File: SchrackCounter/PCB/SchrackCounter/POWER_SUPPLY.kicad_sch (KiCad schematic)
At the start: 14 parts

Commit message: Schematic update
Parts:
- gave numbers to parts that had none: 14
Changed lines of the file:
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@@
 		(on_board yes)
 		(dnp no)
-		(property "Reference" "C?"
+		(property "Reference" "C4"
 			(at 171.45 66.04 0)
 			(effects
@@
 			(project "SchrackCounter"
 				(path "/d96f2ffc-3f4c-4f71-b693-29f6b8c3245d/2b0bd697-1473-4a31-8990-1278f12dea07"
-					(reference "C?")
+					(reference "C4")
 					(unit 1)
 				)
@@
 		(on_board yes)
 		(dnp no)
-		(property "Reference" "C?"
+		(property "Reference" "C7"
 			(at 208.28 66.04 0)
 			(effects
@@
 			(project "SchrackCounter"
 				(path "/d96f2ffc-3f4c-4f71-b693-29f6b8c3245d/2b0bd697-1473-4a31-8990-1278f12dea07"
-					(reference "C?")
+					(reference "C7")
 					(unit 1)
 				)
@@
 		(on_board yes)
 		(dnp no)
-		(property "Reference" "C?"
+		(property "Reference" "C2"
 			(at 125.095 123.19 0)
 			(effects
@@
 			(project "SchrackCounter"
 				(path "/d96f2ffc-3f4c-4f71-b693-29f6b8c3245d/2b0bd697-1473-4a31-8990-1278f12dea07"
-					(reference "C?")
+					(reference "C2")
 					(unit 1)
 				)
@@
 		(on_board yes)
 		(dnp no)
-		(property "Reference" "SW?"
+		(property "Reference" "SW1"
 			(at 200.66 121.92 0)
 			(effects
@@
 			(project "SchrackCounter"
 				(path "/d96f2ffc-3f4c-4f71-b693-29f6b8c3245d/2b0bd697-1473-4a31-8990-1278f12dea07"
-					(reference "SW?")
+					(reference "SW1")
 					(unit 1)
 				)
@@
 		(on_board yes)
 		(dnp no)
-		(property "Reference" "C?"
+		(property "Reference" "C8"
 			(at 217.805 66.04 0)
 			(effects
@@
 			(project "SchrackCounter"
 				(path "/d96f2ffc-3f4c-4f71-b693-29f6b8c3245d/2b0bd697-1473-4a31-8990-1278f12dea07"
-					(reference "C?")
+					(reference "C8")
 					(unit 1)
 				)
@@
 		(on_board yes)
 		(dnp no)
-		(property "Reference" "C?"
+		(property "Reference" "C1"
 			(at 114.935 123.19 0)
 			(effects
@@
 			(project "SchrackCounter"
 				(path "/d96f2ffc-3f4c-4f71-b693-29f6b8c3245d/2b0bd697-1473-4a31-8990-1278f12dea07"
-					(reference "C?")
+					(reference "C1")
 					(unit 1)
 				)
@@
 		(on_board yes)
 		(dnp no)
-		(property "Reference" "L?"
+		(property "Reference" "L1"
 			(at 168.275 54.61 90)
 			(effects
@@
 			(project "SchrackCounter"
 				(path "/d96f2ffc-3f4c-4f71-b693-29f6b8c3245d/2b0bd697-1473-4a31-8990-1278f12dea07"
-					(reference "L?")
+					(reference "L1")
 					(unit 1)
 				)
@@
 		(on_board yes)
 		(dnp no)
-		(property "Reference" "C?"
+		(property "Reference" "C6"
 			(at 198.12 66.04 0)
 			(effects
@@
 			(project "SchrackCounter"
 				(path "/d96f2ffc-3f4c-4f71-b693-29f6b8c3245d/2b0bd697-1473-4a31-8990-1278f12dea07"
-					(reference "C?")
+					(reference "C6")
 					(unit 1)
 				)
@@
 		(on_board yes)
 		(dnp no)
-		(property "Reference" "R?"
+		(property "Reference" "R1"
 			(at 137.16 69.85 90)
 			(effects
@@
 			(project "SchrackCounter"
 				(path "/d96f2ffc-3f4c-4f71-b693-29f6b8c3245d/2b0bd697-1473-4a31-8990-1278f12dea07"
-					(reference "R?")
+					(reference "R1")
 					(unit 1)
 				)
@@
 		(on_board yes)
 		(dnp no)
-		(property "Reference" "C?"
+		(property "Reference" "C3"
 			(at 161.29 66.04 0)
 			(effects
@@
 			(project "SchrackCounter"
 				(path "/d96f2ffc-3f4c-4f71-b693-29f6b8c3245d/2b0bd697-1473-4a31-8990-1278f12dea07"
-					(reference "C?")
+					(reference "C3")
 					(unit 1)
 				)
@@
 		(on_board yes)
 		(dnp no)
-		(property "Reference" "BT?"
+		(property "Reference" "BT1"
 			(at 136.525 123.19 0)
 			(effects
@@
 			(project "SchrackCounter"
 				(path "/d96f2ffc-3f4c-4f71-b693-29f6b8c3245d/2b0bd697-1473-4a31-8990-1278f12dea07"
-					(reference "BT?")
+					(reference "BT1")
 					(unit 1)
 				)
@@
 		(on_board yes)
 		(dnp no)
-		(property "Reference" "R?"
+		(property "Reference" "R2"
 			(at 146.685 69.85 90)
 			(effects
@@
 			(project "SchrackCounter"
 				(path "/d96f2ffc-3f4c-4f71-b693-29f6b8c3245d/2b0bd697-1473-4a31-8990-1278f12dea07"
-					(reference "R?")
+					(reference "R2")
 					(unit 1)
 				)
@@
 		(on_board yes)
 		(dnp no)
-		(property "Reference" "IC?"
+		(property "Reference" "IC1"
 			(at 140.97 50.165 0)
 			(effects
@@
 			(project "SchrackCounter"
 				(path "/d96f2ffc-3f4c-4f71-b693-29f6b8c3245d/2b0bd697-1473-4a31-8990-1278f12dea07"
-					(reference "IC?")
+					(reference "IC1")
 					(unit 1)
 				)
@@
 		(on_board yes)
 		(dnp no)
-		(property "Reference" "C?"
+		(property "Reference" "C5"
 			(at 187.96 66.04 0)
 			(effects
@@
 			(project "SchrackCounter"
 				(path "/d96f2ffc-3f4c-4f71-b693-29f6b8c3245d/2b0bd697-1473-4a31-8990-1278f12dea07"
-					(reference "C?")
-					(unit 1)
-				)
+					(reference "C5")
+					(unit 1)
+				)

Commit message: Schematic update
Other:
- moved on the sheet: BT1, C1, C2, SW1A
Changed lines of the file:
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@@
 	)
 	(junction
-		(at 111.76 129.54)
+		(at 110.49 127)
 		(diameter 0)
 		(color 0 0 0 0)
@@
 	)
 	(junction
-		(at 121.92 119.38)
+		(at 120.65 116.84)
 		(diameter 0)
 		(color 0 0 0 0)
@@
 	)
 	(junction
-		(at 121.92 129.54)
+		(at 120.65 127)
 		(diameter 0)
 		(color 0 0 0 0)
@@
 	)
 	(junction
-		(at 111.76 119.38)
+		(at 110.49 116.84)
 		(diameter 0)
 		(color 0 0 0 0)
@@
 	)
 	(no_connect
-		(at 210.82 119.38)
-	)
-	(wire
-		(pts
-			(xy 100.33 123.19) (xy 107.95 123.19)
+		(at 209.55 120.65)
+	)
+	(wire
+		(pts
+			(xy 99.06 120.65) (xy 106.68 120.65)
 		)
 		(stroke
@@
 	(wire
 		(pts
-			(xy 210.82 119.38) (xy 205.74 119.38)
+			(xy 209.55 120.65) (xy 204.47 120.65)
 		)
 		(stroke
@@
 	(wire
 		(pts
-			(xy 111.76 129.54) (xy 121.92 129.54)
+			(xy 110.49 127) (xy 120.65 127)
 		)
 		(stroke
@@
 	(wire
 		(pts
-			(xy 190.5 116.84) (xy 195.58 116.84)
+			(xy 189.23 118.11) (xy 194.31 118.11)
 		)
 		(stroke
@@
 	(wire
 		(pts
-			(xy 121.92 119.38) (xy 121.92 120.65)
-		)
-		(stroke
-			(width 0)
-			(type default)
-		)
-	)
-	(wire
-		(pts
-			(xy 107.95 129.54) (xy 111.76 129.54)
+			(xy 120.65 116.84) (xy 120.65 118.11)
+		)
+		(stroke
+			(width 0)
+			(type default)
+		)
+	)
+	(wire
+		(pts
+			(xy 106.68 127) (xy 110.49 127)
 		)
 		(stroke
@@
 	(wire
 		(pts
-			(xy 100.33 125.73) (xy 107.95 125.73)
+			(xy 99.06 123.19) (xy 106.68 123.19)
 		)
 		(stroke
@@
 	(wire
 		(pts
-			(xy 107.95 125.73) (xy 107.95 129.54)
+			(xy 106.68 123.19) (xy 106.68 127)
 		)
 		(stroke
@@
 	(wire
 		(pts
-			(xy 107.95 123.19) (xy 107.95 119.38)
+			(xy 106.68 120.65) (xy 106.68 116.84)
 		)
 		(stroke
@@
 	(wire
 		(pts
-			(xy 111.76 119.38) (xy 111.76 120.65)
+			(xy 110.49 116.84) (xy 110.49 118.11)
 		)
 		(stroke
@@
 	(wire
 		(pts
-			(xy 107.95 119.38) (xy 111.76 119.38)
+			(xy 106.68 116.84) (xy 110.49 116.84)
 		)
 		(stroke
@@
 	(wire
 		(pts
-			(xy 121.92 119.38) (xy 133.35 119.38)
+			(xy 120.65 116.84) (xy 132.08 116.84)
 		)
 		(stroke
@@
 	(wire
 		(pts
-			(xy 111.76 119.38) (xy 121.92 119.38)
+			(xy 110.49 116.84) (xy 120.65 116.84)
 		)
 		(stroke
@@
 	(wire
 		(pts
-			(xy 121.92 128.27) (xy 121.92 129.54)
+			(xy 120.65 125.73) (xy 120.65 127)
 		)
 		(stroke
@@
 	(wire
 		(pts
-			(xy 121.92 129.54) (xy 133.35 129.54)
+			(xy 120.65 127) (xy 132.08 127)
 		)
 		(stroke
@@
 	(wire
 		(pts
-			(xy 111.76 128.27) (xy 111.76 129.54)
-		)
-		(stroke
-			(width 0)
-			(type default)
-		)
-	)
-	(wire
-		(pts
-			(xy 209.55 114.3) (xy 205.74 114.3)
+			(xy 110.49 125.73) (xy 110.49 127)
+		)
+		(stroke
+			(width 0)
+			(type default)
+		)
+	)
+	(wire
+		(pts
+			(xy 208.28 115.57) (xy 204.47 115.57)
 		)
 		(stroke
@@
 	(global_label "VBATT"
 		(shape input)
-		(at 190.5 116.84 180)
+		(at 189.23 118.11 180)
 		(fields_autoplaced yes)
 		(effects
@@
 		)
 		(property "Intersheetrefs" "${INTERSHEET_REFS}"
-			(at 184.284 116.84 0)
+			(at 183.014 118.11 0)
 			(effects
 				(font
@@
 	(global_label "VBATT"
 		(shape input)
-		(at 100.33 123.19 180)
+		(at 99.06 120.65 180)
 		(fields_autoplaced yes)
 		(effects
@@
 		)
 		(property "Intersheetrefs" "${INTERSHEET_REFS}"
-			(at 94.114 123.19 0)
+			(at 92.844 120.65 0)
 			(effects
 				(font
@@
 	(symbol
 		(lib_id "power:+5V")
-		(at 209.55 114.3 270)
+		(at 208.28 115.57 270)
 		(unit 1)
 		(exclude_from_sim no)
@@
 		(fields_autoplaced yes)
 		(property "Reference" "#PWR02"
-			(at 205.74 114.3 0)
+			(at 204.47 115.57 0)
 			(effects
 				(font
@@
 		)
 		(property "Value" "+5V"
-			(at 213.36 114.2999 90)
+			(at 212.09 115.5699 90)
 			(effects
 				(font
@@
 		)
 		(property "Footprint" ""
-			(at 209.55 114.3 0)
+			(at 208.28 115.57 0)
 			(effects
 				(font
@@
 		)
 		(property "Datasheet" ""
-			(at 209.55 114.3 0)
+			(at 208.28 115.57 0)
 			(effects
 				(font
@@
 		)
 		(property "Description" "Power symbol creates a global label with name \"+5V\""
-			(at 209.55 114.3 0)
+			(at 208.28 115.57 0)
 			(effects
 				(font
@@
 	(symbol
 		(lib_id "power:GND")
-		(at 100.33 125.73 0)
+		(at 99.06 123.19 0)
 		(unit 1)
 		(exclude_from_sim no)
@@
 		(fields_autoplaced yes)
 		(property "Reference" "#PWR01"
-			(at 100.33 132.08 0)
+			(at 99.06 129.54 0)
 			(effects
 				(font
@@
 		)
 		(property "Value" "GND"
-			(at 100.33 130.81 0)
+			(at 99.06 128.27 0)
 			(effects
 				(font
@@
 		)
 		(property "Footprint" ""
-			(at 100.33 125.73 0)
+			(at 99.06 123.19 0)
 			(effects
 				(font
@@
 		)
 		(property "Datasheet" ""
-			(at 100.33 125.73 0)
+			(at 99.06 123.19 0)
 			(effects
 				(font
@@
 		)
 		(property "Description" "Power symbol creates a global label with name \"GND\" , ground"
-			(at 100.33 125.73 0)
+			(at 99.06 123.19 0)
 			(effects
 				(font
@@
 	(symbol
 		(lib_id "Device:C")
-		(at 121.92 124.46 0)
+		(at 120.65 121.92 0)
 		(unit 1)
 		(exclude_from_sim no)
@@
 		(dnp no)
 		(property "Reference" "C2"
-			(at 125.095 123.19 0)
+			(at 123.825 120.65 0)
 			(effects
 				(font
@@
 		)
 		(property "Value" "100nF"
-			(at 125.095 125.73 0)
+			(at 123.825 123.19 0)
 			(effects
 				(font
@@
 		)
 		(property "Footprint" "Capacitor_SMD:C_0805_2012Metric_Pad1.18x1.45mm_HandSolder"
-			(at 122.8852 128.27 0)
+			(at 121.6152 125.73 0)
 			(effects
 				(font
@@
 		)
 		(property "Datasheet" "~"
-			(at 121.92 124.46 0)
+			(at 120.65 121.92 0)
 			(effects
 				(font
@@
 		)
 		(property "Description" "Unpolarized capacitor"
-			(at 121.92 124.46 0)
+			(at 120.65 121.92 0)
 			(effects
 				(font
@@
 	(symbol
 		(lib_id "Switch:SW_DPDT_x2")
-		(at 200.66 116.84 0)
+		(at 199.39 118.11 0)
 		(unit 1)
 		(exclude_from_sim no)
@@
 		(dnp no)
 		(property "Reference" "SW1"
-			(at 200.66 121.92 0)
+			(at 199.39 123.19 0)
 			(effects
 				(font
@@
 		)
 		(property "Value" "SW_DPDT_x2"
-			(at 200.66 111.76 0)
+			(at 199.39 113.03 0)
 			(effects
 				(font
@@
 		)
 		(property "Footprint" "sumec_brd:Custom_SPDT_4.7mm_Switch"
-			(at 200.66 116.84 0)
+			(at 199.39 118.11 0)
 			(effects
 				(font
@@
 		)
 		(property "Datasheet" "https://cz.mouser.com/ProductDetail/E-Switch/500SSP1S1M2QEA?qs=rR7wk9eDIwofjM3j2mZRnA%3D%3D"
-			(at 200.66 116.84 0)
+			(at 199.39 118.11 0)
 			(effects
 				(font
@@
 		)
 		(property "Description" ""
-			(at 200.66 116.84 0)
+			(at 199.39 118.11 0)
 			(effects
 				(font
@@
 	(symbol
 		(lib_id "Device:C_Polarized")
-		(at 111.76 124.46 0)
+		(at 110.49 121.92 0)
 		(unit 1)
 		(exclude_from_sim no)
@@
 		(dnp no)
 		(property "Reference" "C1"
-			(at 114.935 123.19 0)
+			(at 113.665 120.65 0)
 			(effects
 				(font
@@
 		)
 		(property "Value" "10uF"
-			(at 114.935 125.73 0)
+			(at 113.665 123.19 0)
 			(effects
 				(font
@@
 		)
 		(property "Footprint" "Capacitor_Tantalum_SMD:CP_EIA-3216-18_Kemet-A_Pad1.58x1.35mm_HandSolder"
-			(at 112.7252 128.27 0)
+			(at 111.4552 125.73 0)
 			(effects
 				(font
@@
 		)
 		(property "Datasheet" "~"
-			(at 111.76 124.46 0)
+			(at 110.49 121.92 0)
 			(effects
 				(font
@@
 		)
 		(property "Description" "Polarized capacitor"
-			(at 111.76 124.46 0)
+			(at 110.49 121.92 0)
 			(effects
 				(font
@@
 	(symbol
 		(lib_id "Device:Battery")
-		(at 133.35 124.46 0)
+		(at 132.08 121.92 0)
 		(unit 1)
 		(exclude_from_sim no)
@@
 		(dnp no)
 		(property "Reference" "BT1"
-			(at 136.525 123.19 0)
+			(at 135.255 120.65 0)
 			(effects
 				(font
@@
 		)
 		(property "Value" "Battery"
-			(at 136.525 125.73 0)
+			(at 135.255 123.19 0)
 			(effects
 				(font
@@
 		)
 		(property "Footprint" "Battery:BatteryHolder_Keystone_2462_2xAA - no holes"
-			(at 133.35 122.936 90)
+			(at 132.08 120.396 90)
 			(effects
 				(font
@@
 		)
 		(property "Datasheet" "~"
-			(at 133.35 122.936 90)
+			(at 132.08 120.396 90)
 			(effects
 				(font
@@
 		)
 		(property "Description" "Multiple-cell battery"
-			(at 133.35 124.46 0)
-			(effects
-				(font
+			(at 132.08 121.92 0)
+			(effects
+				(font

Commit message: sleep, overated imo
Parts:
- BT1: footprint Battery:BatteryHolder_Keystone_2462_2xAA - no holes -> Connector_Samtec_HPM_THT:Samtec_HPM-02-01-x-S_Straight_1x02_Pitch5.08mm
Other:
- note added: "Batt connector should probs be in the box but not on the pcb"
- moved on the sheet: BT1, C1, C2, SW1A

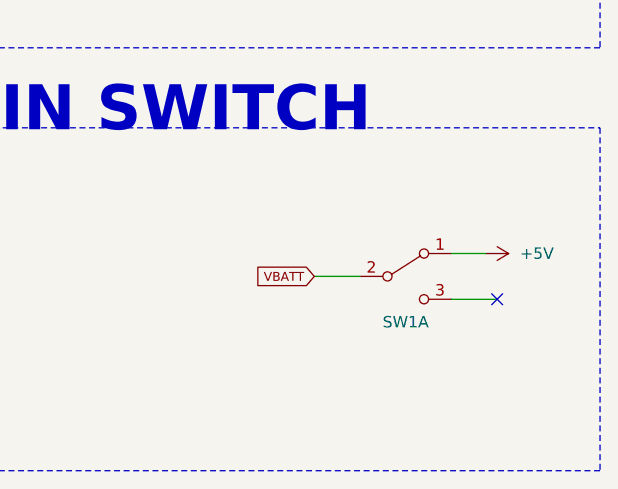
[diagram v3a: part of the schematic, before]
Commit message: SD card addition
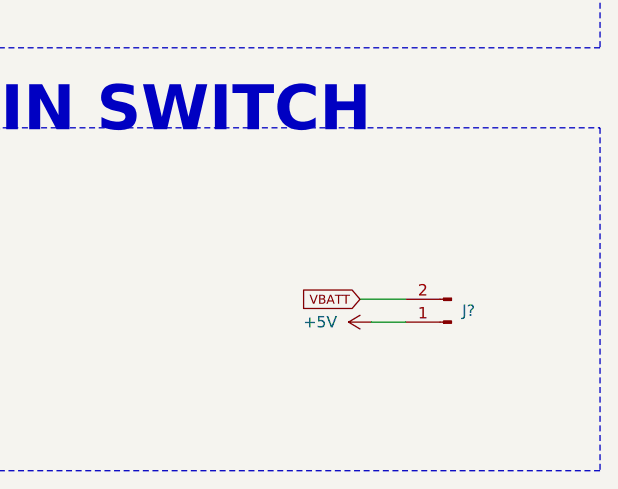
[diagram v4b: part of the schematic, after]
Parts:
- removed SW1: SW_DPDT_x2, sumec_brd:Custom_SPDT_4.7mm_Switch, symbol Switch:SW_DPDT_x2
- added J?: Conn_01x02_Pin, Connector_JST:JST_XH_B2B-XH-A_1x02_P2.50mm_Vertical, symbol Connector:Conn_01x02_Pin
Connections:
- net +5V: now also J?.1 (Pin_1)
- net VBATT: now also J?.2 (Pin_2)
- no-connect marks 1 -> 0
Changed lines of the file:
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@@
 		(color 0 0 0 0)
-	)
-	(no_connect
-		(at 223.52 114.3)
 	)
 	(wire
@@
 	(wire
 		(pts
-			(xy 223.52 114.3) (xy 218.44 114.3)
-		)
-		(stroke
-			(width 0)
-			(type default)
-		)
-	)
-	(wire
-		(pts
 			(xy 185.42 71.12) (xy 185.42 73.66)
 		)
@@
 	(wire
 		(pts
-			(xy 203.2 111.76) (xy 208.28 111.76)
+			(xy 208.28 114.3) (xy 213.36 114.3)
 		)
 		(stroke
@@
 	(wire
 		(pts
-			(xy 222.25 109.22) (xy 218.44 109.22)
+			(xy 209.55 116.84) (xy 213.36 116.84)
 		)
 		(stroke
@@
 	(global_label "VBATT"
 		(shape input)
-		(at 203.2 111.76 180)
+		(at 208.28 114.3 180)
 		(fields_autoplaced yes)
 		(effects
@@
 		)
 		(property "Intersheetrefs" "${INTERSHEET_REFS}"
-			(at 196.984 111.76 0)
+			(at 202.064 114.3 0)
 			(effects
 				(font
@@
 	(symbol
 		(lib_id "power:+5V")
-		(at 222.25 109.22 270)
+		(at 209.55 116.84 90)
 		(unit 1)
 		(exclude_from_sim no)
@@
 		(fields_autoplaced yes)
 		(property "Reference" "#PWR011"
-			(at 218.44 109.22 0)
+			(at 213.36 116.84 0)
 			(effects
 				(font
@@
 		)
 		(property "Value" "+5V"
-			(at 226.06 109.2199 90)
+			(at 205.74 116.8401 90)
 			(effects
 				(font
@@
 		)
 		(property "Footprint" ""
-			(at 222.25 109.22 0)
+			(at 209.55 116.84 0)
 			(effects
 				(font
@@
 		)
 		(property "Datasheet" ""
-			(at 222.25 109.22 0)
+			(at 209.55 116.84 0)
 			(effects
 				(font
@@
 		)
 		(property "Description" "Power symbol creates a global label with name \"+5V\""
-			(at 222.25 109.22 0)
+			(at 209.55 116.84 0)
 			(effects
 				(font
@@
 	)
 	(symbol
-		(lib_id "Switch:SW_DPDT_x2")
-		(at 213.36 111.76 0)
-		(unit 1)
-		(exclude_from_sim no)
-		(in_bom yes)
-		(on_board yes)
-		(dnp no)
-		(property "Reference" "SW1"
-			(at 213.36 116.84 0)
-			(effects
-				(font
-					(face "Bahnschrift")
-					(size 1.27 1.27)
-				)
-			)
-		)
-		(property "Value" "SW_DPDT_x2"
-			(at 213.36 106.68 0)
-			(effects
-				(font
-					(face "Bahnschrift")
-					(size 1.27 1.27)
-				)
-				(hide yes)
-			)
-		)
-		(property "Footprint" "sumec_brd:Custom_SPDT_4.7mm_Switch"
-			(at 213.36 111.76 0)
-			(effects
-				(font
-					(face "Bahnschrift")
-					(size 1.27 1.27)
-				)
-				(hide yes)
-			)
-		)
-		(property "Datasheet" "https://cz.mouser.com/ProductDetail/E-Switch/500SSP1S1M2QEA?qs=rR7wk9eDIwofjM3j2mZRnA%3D%3D"
-			(at 213.36 111.76 0)
-			(effects
-				(font
-					(face "Bahnschrift")
-					(size 1.27 1.27)
-				)
-				(hide yes)
-			)
-		)
-		(property "Description" ""
-			(at 213.36 111.76 0)
-			(effects
-				(font
-					(size 1.27 1.27)
-				)
-				(hide yes)
-			)
-		)
-		(pin "1"
-		)
-		(pin "2"
-		)
-		(pin "3"
-		)
-		(pin "4"
-		)
-		(pin "5"
-		)
-		(pin "6"
-		)
-		(instances
-			(project "SchrackCounter"
-				(path "/d96f2ffc-3f4c-4f71-b693-29f6b8c3245d/2b0bd697-1473-4a31-8990-1278f12dea07"
-					(reference "SW1")
-					(unit 1)
-				)
-			)
-		)
-	)
-	(symbol
 		(lib_id "Device:C")
 		(at 214.63 67.31 0)
@@
 					(unit 1)
 				)
+			)
+		)
+	)
+	(symbol
+		(lib_id "Connector:Conn_01x02_Pin")
+		(at 218.44 116.84 180)
+		(unit 1)
+		(exclude_from_sim no)
+		(in_bom yes)
+		(on_board yes)
+		(dnp no)
+		(property "Reference" "J?"
+			(at 220.345 115.57 0)
+			(effects
+				(font
+					(size 1.27 1.27)
+				)
+			)
+		)
+		(property "Value" "Conn_01x02_Pin"
+			(at 219.075 119.38 0)
+			(effects
+				(font
+					(size 1.27 1.27)
+				)
+				(hide yes)
+			)
+		)
+		(property "Footprint" "Connector_JST:JST_XH_B2B-XH-A_1x02_P2.50mm_Vertical"
+			(at 218.44 116.84 0)
+			(effects
+				(font
+					(size 1.27 1.27)
+				)
+				(hide yes)
+			)
+		)
+		(property "Datasheet" "~"
+			(at 218.44 116.84 0)
+			(effects
+				(font
+					(size 1.27 1.27)
+				)
+				(hide yes)
+			)
+		)
+		(property "Description" "Generic connector, single row, 01x02, script generated"
+			(at 218.44 116.84 0)
+			(effects
+				(font
+					(size 1.27 1.27)
+				)
+				(hide yes)
+			)
+		)
+		(pin "2"
+		)
+		(pin "1"
+		)
+		(instances
+			(project "SchrackCounter"
+				(path "/d96f2ffc-3f4c-4f71-b693-29f6b8c3245d/2b0bd697-1473-4a31-8990-1278f12dea07"
+					(reference "J?")
+					(unit 1)
+				)

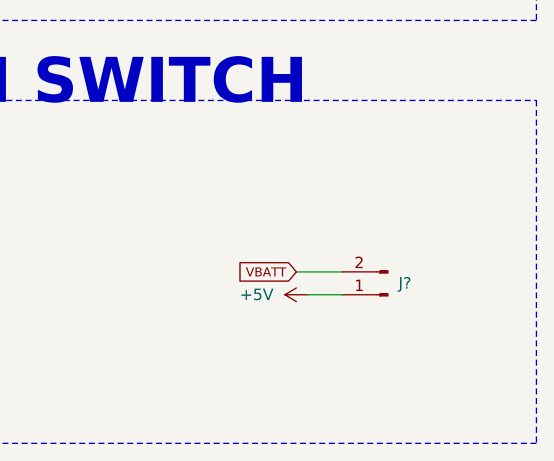
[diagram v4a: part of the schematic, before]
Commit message: Footprint reorder, schematic and pcb update
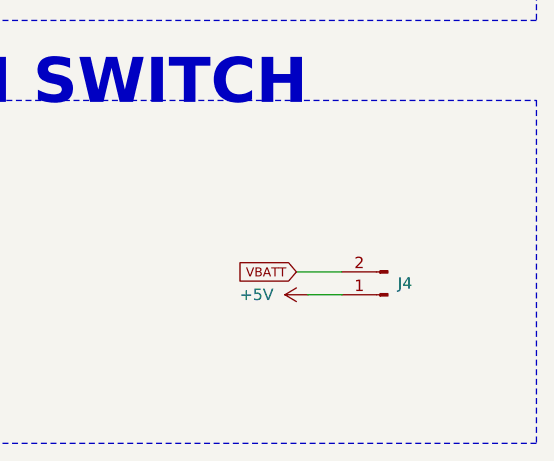
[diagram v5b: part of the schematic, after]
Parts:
- gave numbers to parts that had none: 1
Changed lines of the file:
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@@
 		(on_board yes)
 		(dnp no)
-		(property "Reference" "J?"
+		(property "Reference" "J4"
 			(at 220.345 115.57 0)
 			(effects
@@
 			(project "SchrackCounter"
 				(path "/d96f2ffc-3f4c-4f71-b693-29f6b8c3245d/2b0bd697-1473-4a31-8990-1278f12dea07"
-					(reference "J?")
+					(reference "J4")
 					(unit 1)
 				)

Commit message: PCB update
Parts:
- BT1: footprint Connector_Samtec_HPM_THT:Samtec_HPM-02-01-x-S_Straight_1x02_Pitch5.08mm -> Schrack_brd:SOLDER_PADS
- renumbered J4 to J1
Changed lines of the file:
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@@
 		(dnp no)
 		(fields_autoplaced yes)
-		(property "Reference" "#PWR011"
+		(property "Reference" "#PWR010"
 			(at 213.36 116.84 0)
 			(effects
@@
 			(project "SchrackCounter"
 				(path "/d96f2ffc-3f4c-4f71-b693-29f6b8c3245d/2b0bd697-1473-4a31-8990-1278f12dea07"
-					(reference "#PWR011")
+					(reference "#PWR010")
 					(unit 1)
 				)
@@
 		(on_board yes)
 		(dnp no)
-		(property "Reference" "#PWR010"
+		(property "Reference" "#PWR011"
 			(at 217.17 59.69 0)
 			(effects
@@
 			(project "SchrackCounter"
 				(path "/d96f2ffc-3f4c-4f71-b693-29f6b8c3245d/2b0bd697-1473-4a31-8990-1278f12dea07"
-					(reference "#PWR010")
+					(reference "#PWR011")
 					(unit 1)
 				)
@@
 			)
 		)
-		(property "Footprint" "Connector_Samtec_HPM_THT:Samtec_HPM-02-01-x-S_Straight_1x02_Pitch5.08mm"
+		(property "Footprint" "Schrack_brd:SOLDER_PADS"
 			(at 132.08 119.126 90)
 			(effects
@@
 		(on_board yes)
 		(dnp no)
-		(property "Reference" "J4"
+		(property "Reference" "J1"
 			(at 220.345 115.57 0)
 			(effects
@@
 			(project "SchrackCounter"
 				(path "/d96f2ffc-3f4c-4f71-b693-29f6b8c3245d/2b0bd697-1473-4a31-8990-1278f12dea07"
-					(reference "J4")
-					(unit 1)
-				)
+					(reference "J1")
+					(unit 1)
+				)

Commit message: schematic and board update
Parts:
- removed C3, C5, C6, C7: 22uF, Capacitor_Tantalum_SMD:CP_EIA-2012-12_Kemet-R_Pad1.30x1.05mm_HandSolder, symbol Device:C_Polarized
- removed C4: 100nF.vin, Capacitor_SMD:C_0805_2012Metric_Pad1.18x1.45mm_HandSolder, symbol Device:C
- removed C8: 100nF.vout, Capacitor_SMD:C_0805_2012Metric_Pad1.18x1.45mm_HandSolder, symbol Device:C
- removed IC1: TPS565242DRLR, Package_TO_SOT_SMD:SOT-563, symbol SamacSys_Parts:TPS565242DRLR
- removed L1: 1.5uH, Inductor_SMD:L_Vishay_IHLP-1212, symbol Device:L
- removed R1: 45k, Resistor_SMD:R_0805_2012Metric_Pad1.20x1.40mm_HandSolder, symbol Device:R
- removed R2: 10k, Resistor_SMD:R_0805_2012Metric_Pad1.20x1.40mm_HandSolder, symbol Device:R
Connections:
- net +5V: now also J1.2 (Pin_2); no longer J1.1 (Pin_1)
- net VBATT: now also J1.1 (Pin_1); no longer J1.2 (Pin_2)
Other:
- note removed: "Driving EN high enables the converter."
- note removed: "FeedBack voltage divider, usinf formula from datasheet"
- note removed: "STEPDOWN CONVERTER 3.3V"
